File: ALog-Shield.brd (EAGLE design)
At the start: 53.3 x 78.5 mm, 26 parts, among them U1 DS3231MZ/V+T

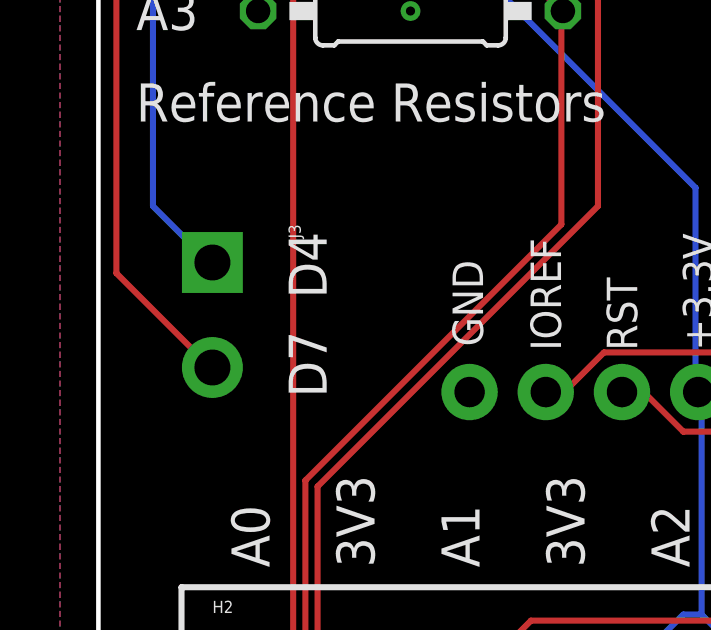
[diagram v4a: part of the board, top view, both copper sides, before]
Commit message: screw terminal + spacing to text
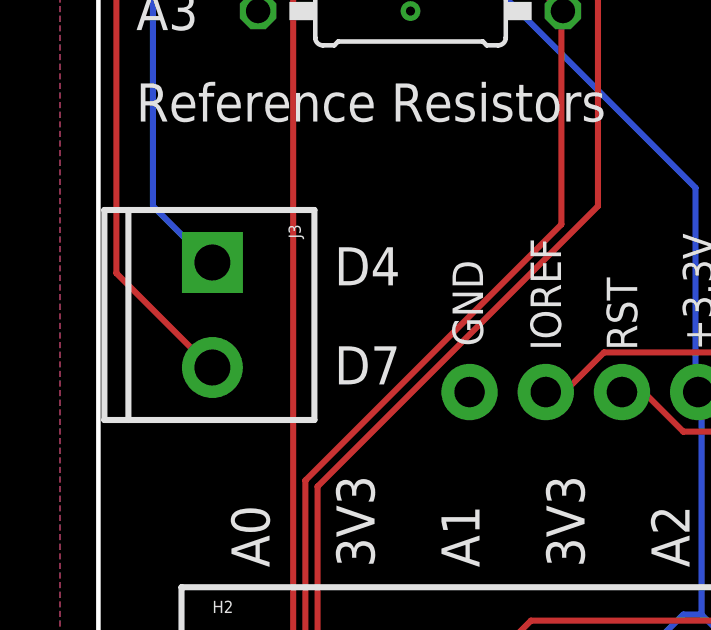
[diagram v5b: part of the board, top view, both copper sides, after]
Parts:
- J3: device SparkFun-Connectors:SCREWTERMINAL-3.5MM-2-NS -> SparkFun-Connectors:SCREWTERMINAL-3.5MM-2
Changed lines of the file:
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@@
 Northern Widget LLC and
 University of Minnesota</text>
-<text x="6.35" y="19.05" size="1.27" layer="21" rot="R270">D4</text>
-<text x="6.35" y="15.748" size="1.27" layer="21" rot="R270">D7</text>
+<text x="7.874" y="17.272" size="1.27" layer="21">D4</text>
+<text x="7.874" y="13.97" size="1.27" layer="21">D7</text>
 </plain>
 <attributes>
@@
 <element name="U$3" library="awickert" package="ALOG_LOG" value="ALOG_LOG" x="19.558" y="35.052" rot="R90"/>
 <element name="LOGO1" library="SparkFun-Aesthetics" package="OSHW-LOGO-L" value="OSHW-LOGOL" x="16.51" y="39.878" rot="R270"/>
-<element name="J3" library="SparkFun-Connectors" package="SCREWTERMINAL-3.5MM-2-NS" value="" x="3.81" y="18.034" rot="R270">
+<element name="J3" library="SparkFun-Connectors" package="SCREWTERMINAL-3.5MM-2" value="" x="3.81" y="18.034" rot="R270">
 <attribute name="PROD_ID" value="CONN-08399" x="3.81" y="18.034" size="1.778" layer="27" rot="R270" display="off"/>
 </element>

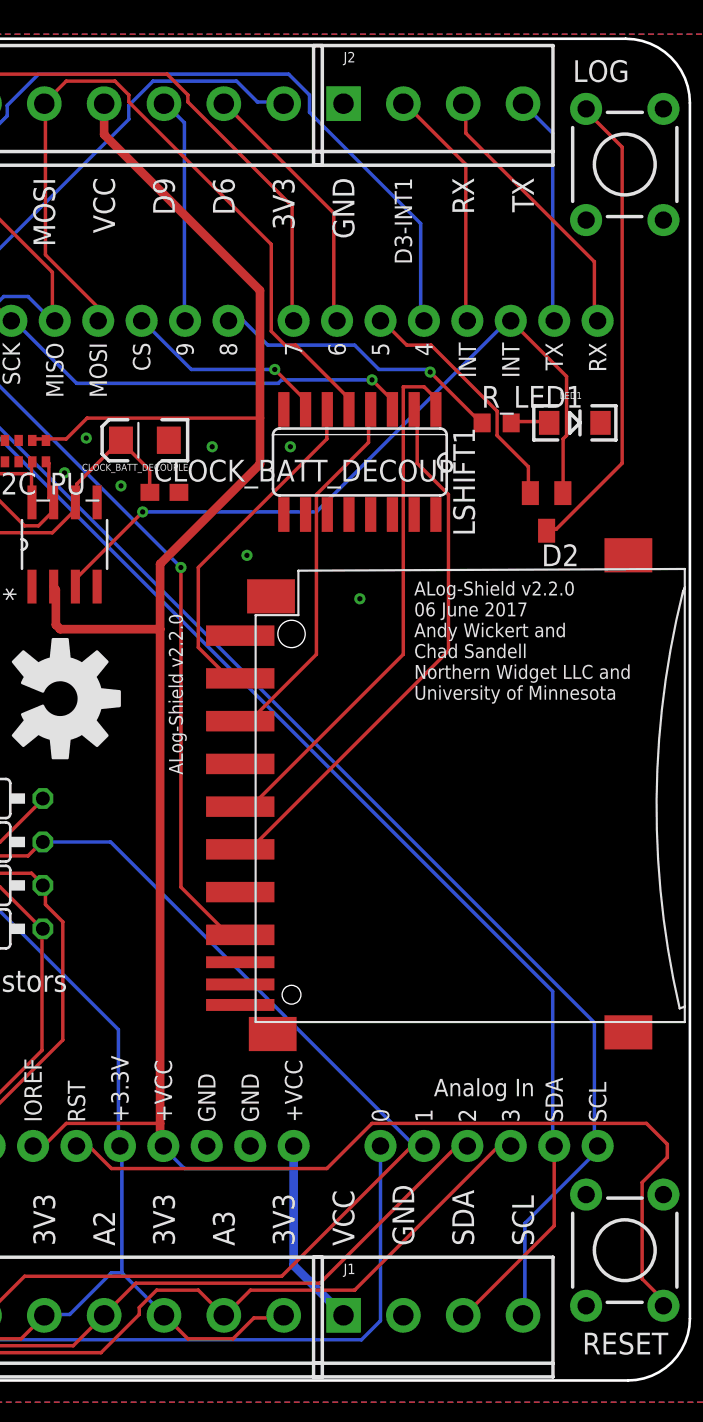
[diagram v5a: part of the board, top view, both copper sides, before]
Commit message: 3V3 (not VDD) and VCC
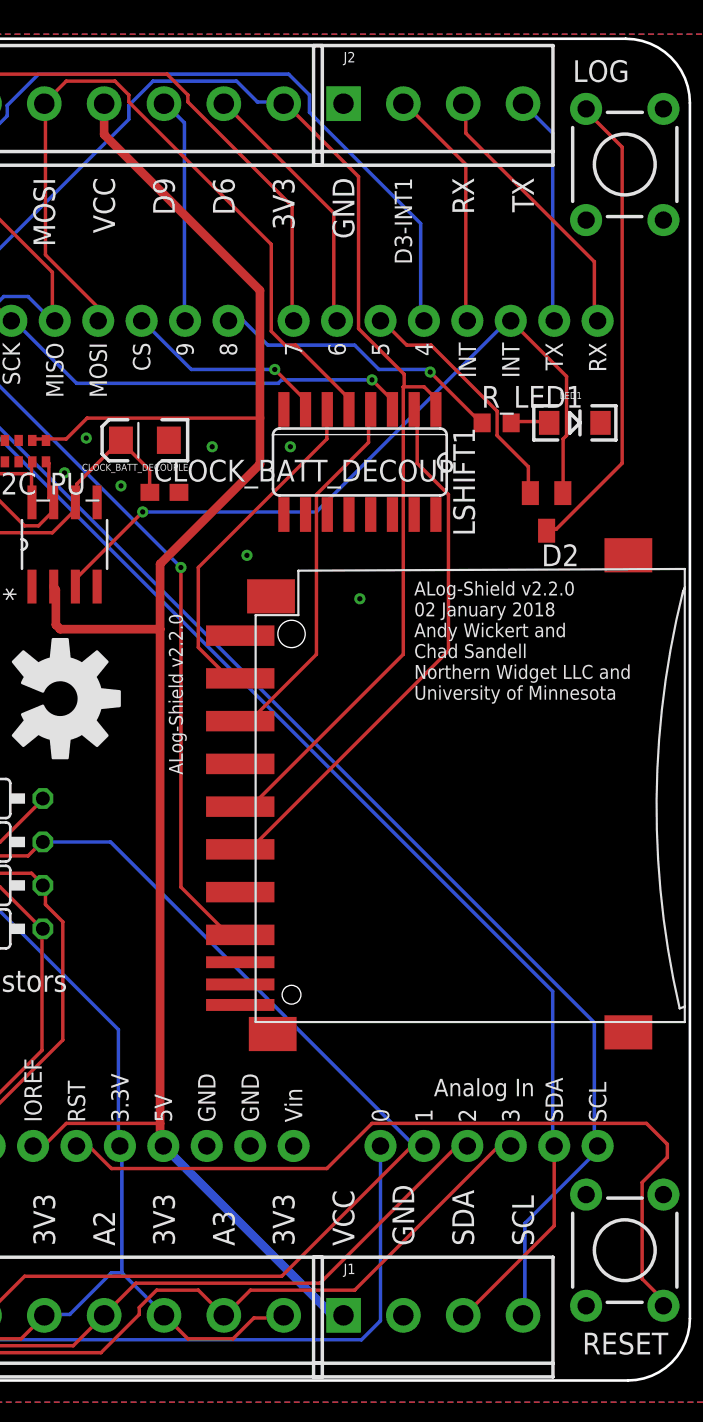
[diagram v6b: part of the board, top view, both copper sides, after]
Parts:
- U$9: value ARDUINO_SHIELD_PIN_PURPOSE -> AWICKERT_ARDUINO_SHIELD_PIN_PURPOSE; device awickert:ARDUINO_SHIELD_PINS_ONLY -> ALog-Shield:AWICKERT_ARDUINO_SHIELD_PINS_ONLY
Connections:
- removed net VDD: LSHIFT1.1, SD1.4
- new net VIN: U$9.VIN
- net +3V3: now also LSHIFT1.1, SD1.4
- net VCC: no longer U$9.VIN
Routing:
- net +3V3: track 124.5 -> 175.7 mm
- net VDD: track 31.7 -> 0.00 mm
- net VCC: track 117.0 -> 112.2 mm
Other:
- board text added: "ALog-Shield v2.2.0 02 January 2018 Andy Wickert and Chad Sandell Northern Widget LLC and University of Minnesota"
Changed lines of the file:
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@@
 <?xml version="1.0" encoding="utf-8"?>
 <!DOCTYPE eagle SYSTEM "eagle.dtd">
-<eagle version="8.3.1">
+<eagle version="8.5.0">
 <drawing>
 <settings>
@@
 <layer number="59" name="tCarbon" color="7" fill="1" visible="no" active="no"/>
 <layer number="60" name="bCarbon" color="7" fill="1" visible="no" active="no"/>
+<layer number="88" name="SimResults" color="9" fill="1" visible="no" active="no"/>
+<layer number="89" name="SimProbes" color="9" fill="1" visible="no" active="no"/>
 <layer number="90" name="Modules" color="7" fill="1" visible="no" active="no"/>
 <layer number="91" name="Nets" color="2" fill="1" visible="no" active="no"/>
@@
 <text x="1.27" y="22.733" size="1.27" layer="21">Reference Resistors</text>
 <text x="37.211" y="39.8145" size="0.8128" layer="21">ALog-Shield v2.2.0
-06 June 2017
+02 January 2018
 Andy Wickert and
 Chad Sandell
@@
 <param name="dpMaxLengthDifference" value="10mm"/>
 <param name="dpGapFactor" value="2.5"/>
-<param name="checkGrid" value="0"/>
 <param name="checkAngle" value="0"/>
 <param name="checkFont" value="1"/>
 <param name="checkRestrict" value="1"/>
+<param name="checkStop" value="0"/>
+<param name="checkValues" value="0"/>
 <param name="useDiameter" value="13"/>
 <param name="maxErrors" value="50"/>
@@
 </autorouter>
 <elements>
-<element name="U$9" library="awickert" package="ARDUINO_SHIELD_PINS_ONLY" value="ARDUINO_SHIELD_PIN_PURPOSE" x="-6.6675" y="64.516" smashed="yes" rot="R270"/>
+<element name="U$9" library="ALog-Shield" package="AWICKERT_ARDUINO_SHIELD_PINS_ONLY" value="AWICKERT_ARDUINO_SHIELD_PIN_PURPOSE" x="-6.6675" y="64.516" smashed="yes" rot="R270"/>
 <element name="LSHIFT1" library="40xx" package="SO16" value="4050D" x="34.036" y="53.721" rot="R180"/>
 <element name="SD1" library="adafruit" package="06132" value="SDMMC06132" x="27.94" y="34.163" rot="R90"/>
@@
 <signal name="VCC">
 <contactref element="U$9" pad="5V"/>
-<contactref element="U$9" pad="VIN"/>
 <contactref element="J1" pad="1"/>
 <contactref element="U1" pad="2"/>
@@
 <wire x1="22.352" y1="47.752" x2="22.352" y2="43.942" width="0.508" layer="1"/>
 <wire x1="22.352" y1="43.942" x2="22.352" y2="15.0368" width="0.508" layer="1"/>
-<wire x1="22.352" y1="15.0368" x2="22.352" y2="13.716" width="0.508" layer="1"/>
 <wire x1="28.194" y1="53.594" x2="22.352" y2="47.752" width="0.508" layer="1"/>
 <wire x1="28.194" y1="63.754" x2="28.194" y2="56.2864" width="0.508" layer="1"/>
 <wire x1="28.194" y1="56.2864" x2="28.194" y2="53.594" width="0.508" layer="1"/>
-<wire x1="22.352" y1="13.716" x2="22.5425" y2="13.716" width="0.508" layer="1"/>
-<wire x1="30.1625" y1="13.716" x2="30.1625" y2="12.3952" width="0.508" layer="16"/>
-<wire x1="30.1625" y1="12.3952" x2="30.1625" y2="6.7275" width="0.508" layer="16"/>
-<wire x1="30.1625" y1="6.7275" x2="33.08" y2="3.81" width="0.508" layer="16"/>
 <wire x1="16.51" y1="43.942" x2="22.352" y2="43.942" width="0.508" layer="1"/>
 <wire x1="16.256" y1="44.196" x2="16.51" y2="43.942" width="0.508" layer="1"/>
@@
 <wire x1="22.352" y1="15.0368" x2="16.8656" y2="15.0368" width="0.2032" layer="1"/>
 <wire x1="15.0368" y1="13.8176" x2="14.9225" y2="13.716" width="0.2032" layer="1"/>
-<wire x1="23.7744" y1="12.3952" x2="30.1625" y2="12.3952" width="0.2032" layer="16"/>
-<wire x1="22.5552" y1="13.6144" x2="23.7744" y2="12.3952" width="0.2032" layer="16"/>
-<wire x1="22.5552" y1="13.6144" x2="22.5425" y2="13.716" width="0.2032" layer="16"/>
+<wire x1="22.352" y1="15.0368" x2="22.352" y2="13.9065" width="0.508" layer="1"/>
+<wire x1="22.352" y1="13.9065" x2="22.5425" y2="13.716" width="0.508" layer="1"/>
+<wire x1="22.5425" y1="13.716" x2="32.4485" y2="3.81" width="0.508" layer="16"/>
+<wire x1="32.4485" y1="3.81" x2="33.08" y2="3.81" width="0.508" layer="16"/>
 </signal>
 <signal name="DI">
@@
 <wire x1="29.464" y1="74.7776" x2="29.58" y2="74.676" width="0.2032" layer="16"/>
 <wire x1="8.7376" y1="61.976" x2="8.5725" y2="61.976" width="0.2032" layer="16"/>
+<contactref element="LSHIFT1" pad="1"/>
+<contactref element="SD1" pad="4"/>
+<wire x1="38.4048" y1="57.5056" x2="38.4048" y2="56.896" width="0.2032" layer="1"/>
+<wire x1="37.7952" y1="58.1152" x2="38.4048" y2="57.5056" width="0.2032" layer="1"/>
+<wire x1="36.576" y1="58.1152" x2="37.7952" y2="58.1152" width="0.2032" layer="1"/>
+<wire x1="36.576" y1="42.4688" x2="36.576" y2="58.1152" width="0.2032" layer="1"/>
+<wire x1="27.8384" y1="33.7312" x2="36.576" y2="42.4688" width="0.2032" layer="1"/>
+<wire x1="27.2288" y1="33.7312" x2="27.8384" y2="33.7312" width="0.2032" layer="1"/>
+<wire x1="27.2288" y1="33.7312" x2="27.04" y2="33.563" width="0.2032" layer="1"/>
+<wire x1="38.4048" y1="56.896" x2="38.481" y2="56.7944" width="0.2032" layer="1"/>
+<wire x1="36.6268" y1="58.8518" x2="36.6268" y2="58.1406" width="0.2032" layer="1"/>
+<wire x1="33.9598" y1="61.5188" x2="36.6268" y2="58.8518" width="0.2032" layer="1"/>
+<wire x1="33.9598" y1="70.4088" x2="33.9598" y2="61.5188" width="0.2032" layer="1"/>
+<wire x1="29.6926" y1="74.676" x2="33.9598" y2="70.4088" width="0.2032" layer="1"/>
+<wire x1="36.6268" y1="58.1406" x2="36.576" y2="58.1152" width="0.2032" layer="1"/>
+<wire x1="29.6926" y1="74.676" x2="29.58" y2="74.676" width="0.2032" layer="1"/>
 </signal>
 <signal name="SCL">
@@
 <wire x1="27.0256" y1="41.2496" x2="27.04" y2="41.063" width="0.2032" layer="1"/>
 </signal>
-<signal name="VDD">
-<contactref element="LSHIFT1" pad="1"/>
-<contactref element="SD1" pad="4"/>
-<wire x1="38.4048" y1="57.5056" x2="38.4048" y2="56.896" width="0.2032" layer="1"/>
-<wire x1="37.7952" y1="58.1152" x2="38.4048" y2="57.5056" width="0.2032" layer="1"/>
-<wire x1="36.576" y1="58.1152" x2="37.7952" y2="58.1152" width="0.2032" layer="1"/>
-<wire x1="36.576" y1="42.4688" x2="36.576" y2="58.1152" width="0.2032" layer="1"/>
-<wire x1="27.8384" y1="33.7312" x2="36.576" y2="42.4688" width="0.2032" layer="1"/>
-<wire x1="27.2288" y1="33.7312" x2="27.8384" y2="33.7312" width="0.2032" layer="1"/>
-<wire x1="38.4048" y1="56.896" x2="38.481" y2="56.7944" width="0.2032" layer="1"/>
-<wire x1="27.2288" y1="33.7312" x2="27.04" y2="33.563" width="0.2032" layer="1"/>
-</signal>
 <signal name="A1">
 <contactref element="U$9" pad="A1"/>
@@
 <wire x1="3.6576" y1="14.6304" x2="3.81" y2="14.534" width="0.2032" layer="1"/>
 </signal>
+<signal name="VIN">
+<contactref element="U$9" pad="VIN"/>
+</signal>
 </signals>

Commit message: Beta for review
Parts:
- added U$1: NWLOGO_MED, awickert:NWLOGO_MED
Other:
- board text added: "Developed in part at the University of Minnesota in parntnership with Northern Widget LLC"
- board text added: "TM"
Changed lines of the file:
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@@
 <?xml version="1.0" encoding="utf-8"?>
 <!DOCTYPE eagle SYSTEM "eagle.dtd">
-<eagle version="8.5.0">
+<eagle version="8.3.1">
 <drawing>
 <settings>
@@
 <text x="23.6855" y="35.433" size="0.8128" layer="21" rot="R90">ALog-Shield v2.2.0</text>
 <text x="1.27" y="22.733" size="1.27" layer="21">Reference Resistors</text>
-<text x="37.211" y="39.8145" size="0.8128" layer="21">ALog-Shield v2.2.0
+<text x="35.687" y="38.7985" size="0.8128" layer="21">ALog-Shield v2.2.0
 02 January 2018
 Andy Wickert and
@@
 <text x="7.874" y="17.272" size="1.27" layer="21">D4</text>
 <text x="7.874" y="13.97" size="1.27" layer="21">D7</text>
+<text x="23.368" y="70.358" size="1.016" layer="22" rot="MR180">Developed in part at the
+University of Minnesota in
+parntnership with
+Northern Widget LLC</text>
+<text x="3.81" y="69.596" size="0.6096" layer="22" rot="MR0">TM</text>
 </plain>
 <attributes>
@@
 <param name="dpMaxLengthDifference" value="10mm"/>
 <param name="dpGapFactor" value="2.5"/>
+<param name="checkGrid" value="0"/>
 <param name="checkAngle" value="0"/>
 <param name="checkFont" value="1"/>
 <param name="checkRestrict" value="1"/>
-<param name="checkStop" value="0"/>
-<param name="checkValues" value="0"/>
 <param name="useDiameter" value="13"/>
 <param name="maxErrors" value="50"/>
@@
 </element>
 <element name="LOG" library="SparkFun-Electromechanical" package="TACTILE-PTH" value="LOG" x="49.53" y="71.12" smashed="yes" rot="R270">
-<attribute name="NAME" x="46.482" y="75.946" size="1.27" layer="21" ratio="10"/>
+<attribute name="NAME" x="47.498" y="75.946" size="1.27" layer="21" ratio="10"/>
 <attribute name="PROD_ID" value=" SWCH-08441" x="-179.705" y="172.72" size="1.778" layer="27" rot="R270" display="off"/>
 </element>
@@
 <attribute name="PROD_ID" value="CONN-08399" x="3.81" y="18.034" size="1.778" layer="27" rot="R270" display="off"/>
 </element>
+<element name="U$1" library="awickert" package="NWLOGO_MED" value="NWLOGO_MED" x="7.874" y="67.818" rot="MR0"/>
 </elements>
 <signals>
